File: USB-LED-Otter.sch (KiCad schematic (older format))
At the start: 14 parts, among them J1 USB, J2 PAD, J3 LED, J4 PAD, J5 PAD, SW1 DFU, U1 MCP1700-3302E_SOT23, U2 STM32F072C8Ux

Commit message: added example code
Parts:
- removed U2: STM32F072C8Ux, otter:QFN-48-1EP_7x7mm_P0.5mm_EP2.6x2.6mm, symbol MCU_ST_STM32F0:STM32F072C8Ux
- added U2: STM32F072CBUx, otter:QFN-48-1EP_7x7mm_P0.5mm_EP2.6x2.6mm, symbol MCU_ST_STM32F0:STM32F072CBUx
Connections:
- net +3V3: now also U2.1 (VBAT), U2.24 (VDD), U2.36 (VDDIO2), U2.48 (VDD), U2.9 (VDDA)
- net GND: now also U2.23 (VSS), U2.35 (VSS), U2.47 (VSS), U2.49 (VSS), U2.8 (VSSA)
- net LED: now also U2.45 (PB8)
- net SCK: now also U2.39 (PB3)
- net SCL: now also U2.41 (PB5), U2.42 (PB6)
- net SDA: now also U2.40 (PB4), U2.43 (PB7)
- net SWCLK: now also U2.37 (PA14)
- net SWDIO: now also U2.34 (PA13)
- net USB_N: now also U2.32 (PA11)
- net USB_P: now also U2.33 (PA12)
- net at R1.1, SW1.1: now also U2.44 (BOOT0), U2.46 (PB9)
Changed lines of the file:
@@
 $EndDescr
-$Comp
-L MCU_ST_STM32F0:STM32F072C8Ux U2
-U 1 1 5DAD86AD
-P 5850 3150
-F 0 "U2" H 5800 4828 50  0000 C CNN
-F 1 "STM32F072C8Ux" H 5800 4737 50  0000 C CNN
-F 2 "otter:QFN-48-1EP_7x7mm_P0.5mm_EP2.6x2.6mm" H 5250 1750 50  0001 R CNN
-F 3 "http://www.st.com/st-web-ui/static/active/en/resource/technical/document/datasheet/DM00090510.pdf" H 5850 3150 50  0001 C CNN
-	1    5850 3150
-	1    0    0    -1
-$EndComp
 $Comp
 L Regulator_Linear:MCP1700-3302E_SOT23 U1
@@
 Text GLabel 2450 3100 2    50   Input ~ 0
 USB_N
-Wire Wire Line
-	6050 1650 5950 1650
-Connection ~ 5750 1650
-Wire Wire Line
-	5750 1650 5650 1650
 Connection ~ 5850 1650
-Wire Wire Line
-	5850 1650 5750 1650
-Connection ~ 5950 1650
-Wire Wire Line
-	5950 1650 5850 1650
-Wire Wire Line
-	6050 4650 5950 4650
-Connection ~ 5750 4650
-Wire Wire Line
-	5750 4650 5650 4650
 Connection ~ 5850 4650
-Wire Wire Line
-	5850 4650 5750 4650
-Connection ~ 5950 4650
-Wire Wire Line
-	5950 4650 5850 4650
 $Comp
 L power:GND #PWR0108
@@
 Text GLabel 6450 4350 2    50   Input ~ 0
 SWCLK
+$Comp
+L MCU_ST_STM32F0:STM32F072CBUx U2
+U 1 1 5DD36C6F
+P 5850 3150
+F 0 "U2" H 5800 4831 50  0000 C CNN
+F 1 "STM32F072CBUx" H 5800 4740 50  0000 C CNN
+F 2 "otter:QFN-48-1EP_7x7mm_P0.5mm_EP2.6x2.6mm" H 5250 1750 50  0001 R CNN
+F 3 "http://www.st.com/st-web-ui/static/active/en/resource/technical/document/datasheet/DM00090510.pdf" H 5850 3150 50  0001 C CNN
+	1    5850 3150
+	1    0    0    -1
+$EndComp
+Wire Wire Line
+	5750 1650 5850 1650
+Wire Wire Line
+	5750 4650 5850 4650
+Wire Wire Line
+	5650 4650 5750 4650
+Wire Wire Line
+	5850 4650 5950 4650
+Connection ~ 5750 4650
+Connection ~ 5950 4650
+Wire Wire Line
+	5950 4650 6050 4650
+Wire Wire Line
+	5650 1650 5750 1650
+Wire Wire Line
+	5850 1650 5950 1650
+Connection ~ 5750 1650
+Wire Wire Line
+	5750 1650 5850 1650
+Connection ~ 5950 1650
+Wire Wire Line
+	5950 1650 6050 1650
 $EndSCHEMATC

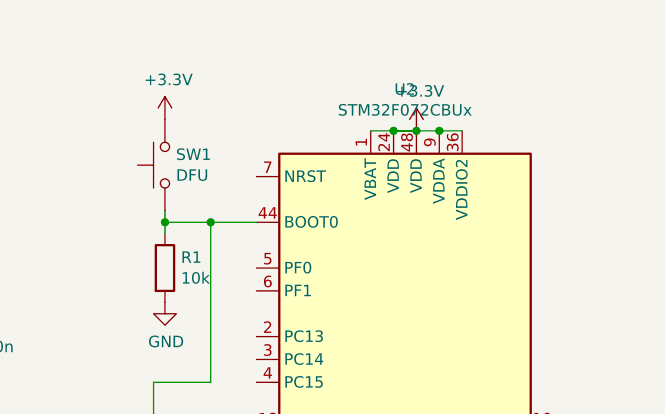
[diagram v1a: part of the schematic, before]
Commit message: added bom
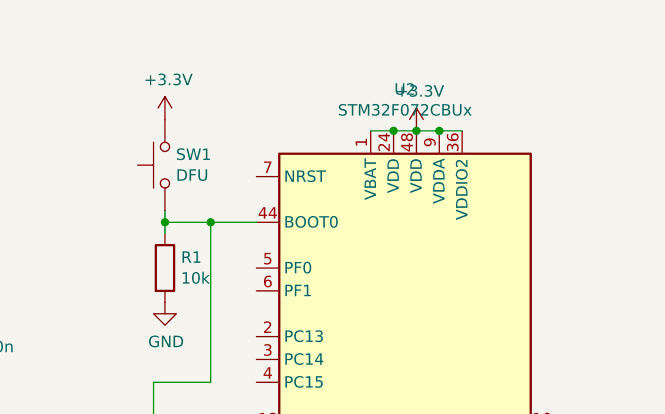
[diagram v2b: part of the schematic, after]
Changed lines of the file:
@@
 	5850 1650 5950 1650
 Connection ~ 5750 1650
-Wire Wire Line
-	5750 1650 5850 1650
 Connection ~ 5950 1650
 Wire Wire Line
